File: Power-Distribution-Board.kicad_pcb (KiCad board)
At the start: 2 copper layers, 12 parts, among them J1 XT60PB-F, J10 XT30UPB-F, J11 XT30UPB-F, J12 XT90PB-F, J2 XT30UPB-F, J3 XT30UPB-F, J4 XT30UPB-F, J5 XT30UPB-F, J6 XT30UPB-F, J7 XT30UPB-F, J8 XT30UPB-F, J9 XT30UPB-F

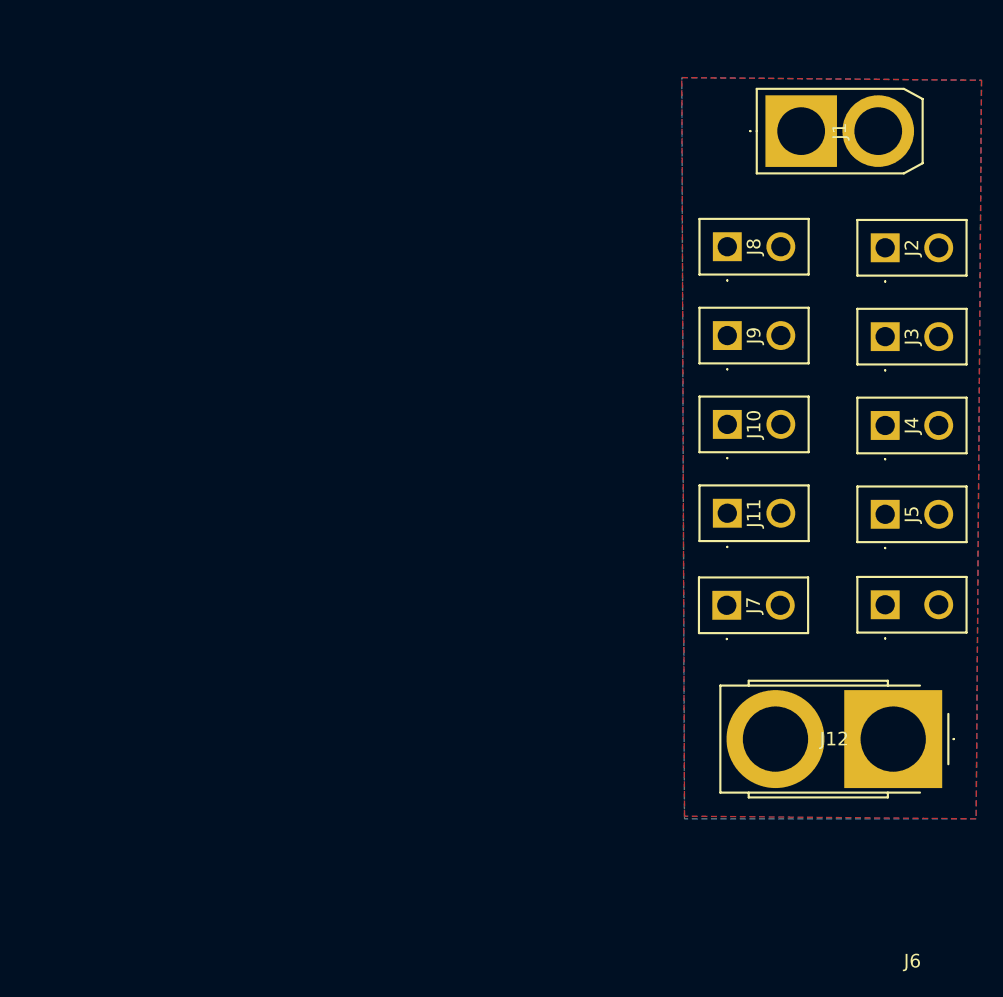
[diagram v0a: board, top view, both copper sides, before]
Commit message: XT90 fully transitioned to male
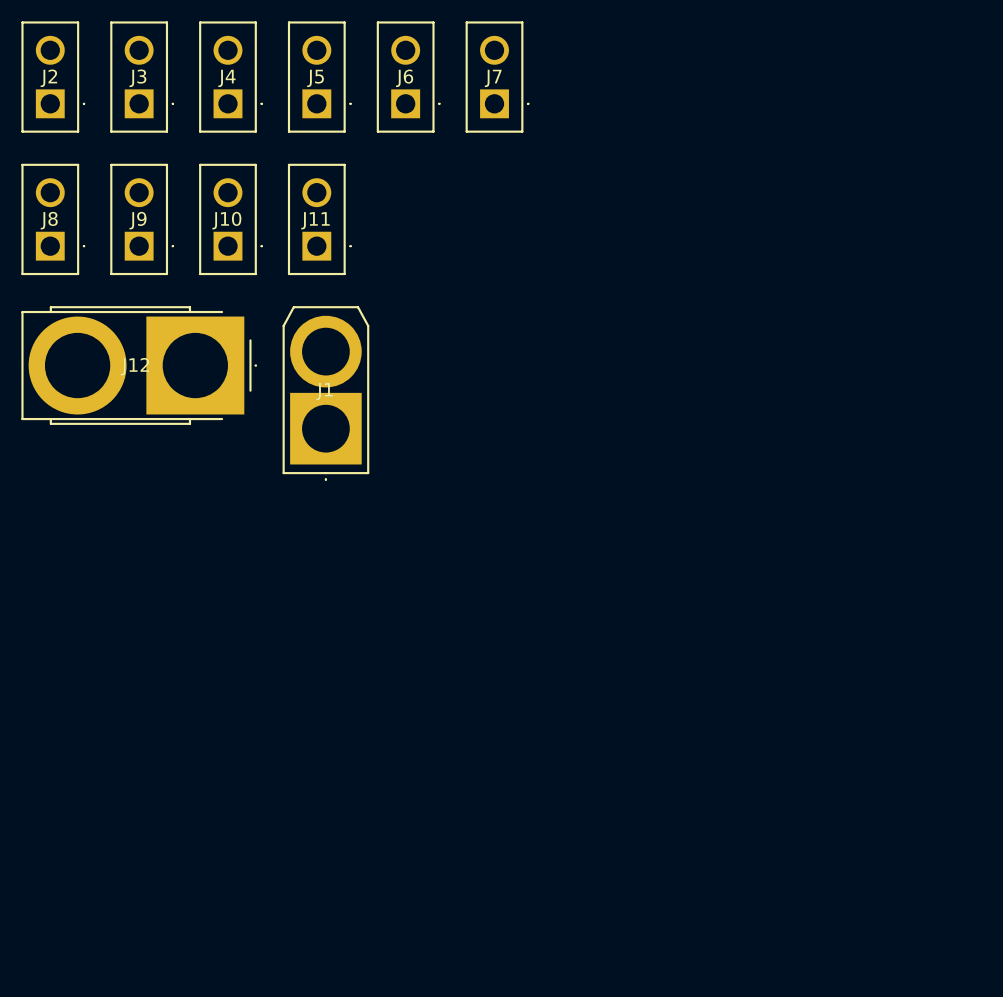
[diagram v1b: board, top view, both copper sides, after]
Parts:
- J12: value XT90PB-F -> XT90PB-M; footprint XT90PB-F:XT90PBF -> XT90PB-M:XT90PBM
- moved J2 79.2 mm to (104.0, 58.7), turned to 0 degrees
- moved J12 74.0 mm to (117.5, 83.2)
- moved J3 73.0 mm to (112.3, 58.7), turned to 0 degrees
- moved J4 68.4 mm to (120.6, 58.7), turned to 0 degrees
- moved J5 65.5 mm to (128.9, 58.7), turned to 0 degrees
- moved J6 64.8 mm to (137.2, 58.7), turned to 0 degrees
- moved J8 63.3 mm to (104.0, 72.0), turned to 0 degrees
- moved J9 55.6 mm to (112.3, 72.0), turned to 0 degrees
- moved J1 52.4 mm to (129.8, 89.0), turned to 0 degrees
- moved J7 51.6 mm to (145.5, 58.7), turned to 0 degrees
- moved J10 49.5 mm to (120.6, 72.0), turned to 0 degrees
- moved J11 45.8 mm to (128.9, 72.0), turned to 0 degrees
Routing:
- removed copper zone on B.Cu, net (none)
- removed copper zone on F.Cu, net (none)
